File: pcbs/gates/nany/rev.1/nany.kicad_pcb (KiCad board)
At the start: 2 copper layers, 12.7 x 7.6 mm, 8 parts, among them J1 Conn_01x03, J2 Conn_01x03, Q1 BSS84, Q2 BSS84, Q3 2N7002, Q4 2N7002

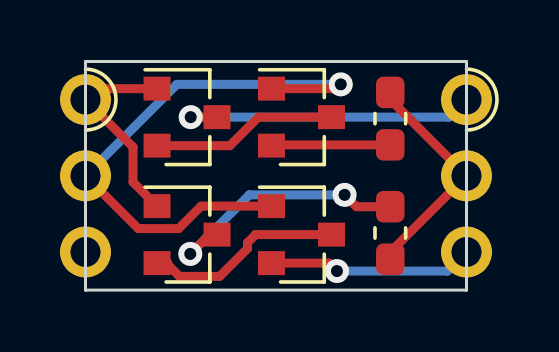
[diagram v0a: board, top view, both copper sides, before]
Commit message: tested rev.0 pcbs and added results to doc
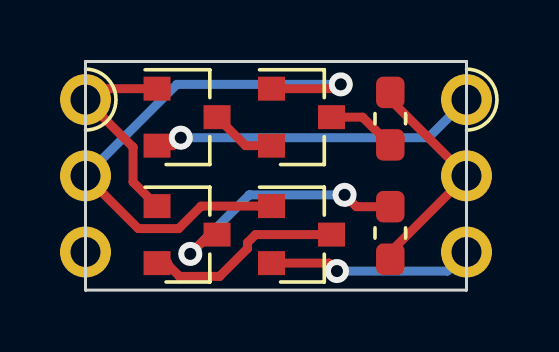
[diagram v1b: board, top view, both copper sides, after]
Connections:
- Q1 pad 2: Net-(Q1-Pad2) -> Vdd
- Q1 pad 3: Vdd -> Net-(Q1-Pad3)
- Q2 pad 2: Net-(Q2-Pad2) -> Net-(Q1-Pad3)
- Q2 pad 3: Net-(Q1-Pad2) -> Net-(Q2-Pad3)
- R1 pad 1: Net-(Q2-Pad2) -> Net-(Q2-Pad3)
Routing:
- net Net-(Q1-Pad2): track 6.21 -> 0.00 mm
- net Net-(Q2-Pad2): track 3.97 -> 0.00 mm
- net Net-(Q2-Pad3): track 0.00 -> 2.34 mm
- net Net-(Q1-Pad3): track 0.00 -> 2.21 mm
